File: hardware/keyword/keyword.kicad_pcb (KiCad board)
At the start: 2 copper layers, 42.3 x 19 mm, 60 parts, among them U1 SZYY0402Y_C434450, U11 STM32WB55RGVx, U12 MLPF-WB-04D3, U13 YZ13515055F-02025-02, U15 YZ13515055F-02025-02, U16 XRTC252012S2R2MBCA, U17 SZYY0402Y_C434450, U18 TPS631000DRLR, U2 TPD2EUSB30, U3 NX2012SA-32.768KHZ-STD-MUB-2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

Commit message: add in stuff
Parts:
- added CN1: YZ00615050R-08, TestPoint:TestPoint_Pad_D2.0mm, F.Cu at (205.1, 74.2)
- added CN2: YZ00615050R-08, lcsc:TESTPOINT-SMD_BD2.0-H5.0, F.Cu at (195.2, 74.4)
- added CN3: YZ00615050R-08, lcsc:TESTPOINT-SMD_BD2.0-H5.0, F.Cu at (195.2, 89.8)
- added CN4: YZ00615050R-08, lcsc:TESTPOINT-SMD_BD2.0-H5.0, F.Cu at (179.8, 89.8)
- added CN5: YZ00615050R-08, TestPoint:TestPoint_Pad_D2.0mm, F.Cu at (205.2, 89.6)
- added CN6: YZ00615050R-08, TestPoint:TestPoint_Pad_D2.0mm, F.Cu at (220.6, 89.6)
- added R11: 2.2K, Resistor_SMD:R_0402_1005Metric, F.Cu at (220.6, 81.7)
- added R8: 2.2K, Resistor_SMD:R_0402_1005Metric, F.Cu at (209.1, 89.6)
- added TP6: TestPoint, TestPoint:TestPoint_Pad_D1.5mm, F.Cu at (205.2, 83.7)
- added TP7: TestPoint, TestPoint:TestPoint_Pad_D1.5mm, F.Cu at (205.2, 86.2)
- added TP8: TestPoint, TestPoint:TestPoint_Pad_D1.5mm, F.Cu at (220.6, 83.8)
- added TP9: TestPoint, TestPoint:TestPoint_Pad_D1.5mm, F.Cu at (220.6, 86.3)
- added U19: YZ37215050R-02025-05, lcsc:SMD_2P_YZ37215050R-02025-05, F.Cu at (195.2, 85.2)
- added U20: YZ37215050R-02025-05, lcsc:SMD_2P_YZ37215050R-02025-05, F.Cu at (179.8, 85.2)
- C16, C17, C18, C19, C20, C23, R4, R5, R6, R7, U16, U17, U8: moved to B.Cu
- TP1, TP2, TP3: footprint TestPoint:TestPoint_Pad_D2.0mm -> TestPoint:TestPoint_Pad_D1.5mm; moved to B.Cu
- TP4, TP5: footprint TestPoint:TestPoint_Pad_3.0x3.0mm -> TestPoint:TestPoint_Pad_2.0x2.0mm; moved to B.Cu
- moved TP4 92.4 mm to (185.8, 89.8)
- moved TP5 90.7 mm to (189.2, 89.8), turned to -90 degrees
- moved C35 35.6 mm to (207.9, 84.9), turned to -90 degrees
- moved AE1 23.7 mm to (220.2, 73.5), turned to 0 degrees
- moved C6 18.5 mm to (217.5, 89.5), turned to -135 degrees
- moved C9 18.5 mm to (219.0, 88.0), turned to -135 degrees
- moved U1 17.9 mm to (215.1, 90.4), turned to 180 degrees
- moved TP1 17.2 mm to (205.7, 85.3), turned to 90 degrees
- moved TP2 16.3 mm to (209.1, 89.2), turned to 90 degrees
- moved L2 15.8 mm to (205.8, 77.0), turned to 90 degrees
- moved R3 15.6 mm to (215.7, 88.9), turned to 90 degrees
- moved C36 15.3 mm to (218.9, 85.0), turned to -90 degrees
- moved C32 15.1 mm to (214.0, 73.9), turned to 90 degrees
- moved X1 15.0 mm to (211.3, 74.5), turned to 45 degrees
- moved C31 15.0 mm to (212.1, 89.5), turned to 180 degrees
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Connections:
- U11 pad 5: /BOOT -> unconnected-(U11-PH3-Pad5)
- U11 pad 6: unconnected-(U11-PB8-Pad6) -> /SDA
- U11 pad 7: unconnected-(U11-PB9-Pad7) -> /SCL
- U11 pad 8: /RESET -> unconnected-(U11-NRST-Pad8)
- U13 pad 2: /SDA3 -> /SDA
- U15 pad 1: /SCL3 -> /SCL
- U2 pad 1: /DP -> /DN
- U2 pad 2: /DN -> /DP
- U4 pad 2: /SDA1 -> /SDA
- U5 pad 1: /SCL1 -> /SCL
- U6 pad 2: /SDA2 -> /SDA
- U7 pad 1: /SCL2 -> /SCL
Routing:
- net /SCL: track 0.00 -> 57.1 mm, vias 0 -> 3
- net +3.3V: track 0.00 -> 52.4 mm, vias 0 -> 12
- net /SDA: track 0.00 -> 52.1 mm, vias 0 -> 6
- net VCC: track 0.00 -> 27.6 mm, vias 0 -> 4
- net Net-(C18-Pad1): track 0.00 -> 23.3 mm, vias 0 -> 4
- net GND: track 0.00 -> 18.2 mm, vias 0 -> 33
- net /DP: track 0.00 -> 17.0 mm
- net /DN: track 0.00 -> 16.9 mm
- net Net-(U8-TS): track 0.00 -> 12.4 mm, vias 0 -> 2
- net VBUS: track 0.00 -> 10.0 mm, vias 0 -> 2
- net /HXOUT: track 0.00 -> 6.10 mm
- net /SWCLK: track 0.00 -> 6.06 mm, vias 0 -> 1
- net Net-(C19-Pad1): track 0.00 -> 4.91 mm
- net /SWDIO: track 0.00 -> 4.72 mm, vias 0 -> 1
- net Net-(AE1-ANT): track 0.00 -> 3.86 mm
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- added copper zone on In2.Cu, net +3.3V
- added copper zone on B.Cu, net GND
- added copper zone on F.Cu, net GND
- added copper zone on In1.Cu, net GND
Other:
- board size 42.3 x 19 mm -> 44.4 x 19.2 mm
- copper layers 2 -> 4

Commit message: aa
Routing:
- net +3.3V: track 52.4 -> 53.7 mm, vias 12 -> 13
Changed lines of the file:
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@@
+	)
+	(segment
+		(start 216.9 78.405)
+		(end 216.195 77.7)
+		(width 0.2)
+		(layer "F.Cu")
+		(net 6)
 	)
 	(segment
@@
 	)
 	(segment
+		(start 216.9 78.7)
+		(end 216.9 78.405)
+		(width 0.2)
+		(layer "F.Cu")
+		(net 6)
+	)
+	(segment
 		(start 209.635437 79.661898)
 		(end 209 79.026461)
@@
 	(via
 		(at 218.9 83.7)
+		(size 0.6)
+		(drill 0.3)
+		(layers "F.Cu" "B.Cu")
+		(net 6)
+	)
+	(via
+		(at 216.9 78.7)
 		(size 0.6)
 		(drill 0.3)
@@
 	)
 	(zone
+		(net 2)
+		(net_name "GND")
+		(layer "F.Cu")
+		(name "$teardrop_padvia$")
+		(hatch none 0.1)
+		(priority 30001)
+		(attr
+			(teardrop
+				(type padvia)
+			)
+		)
+		(connect_pads yes
+			(clearance 0)
+		)
+		(min_thickness 0.0254)
+		(filled_areas_thickness no)
+		(fill yes
+			(thermal_gap 0.5)
+			(thermal_bridge_width 0.5)
+			(island_removal_mode 1)
+			(island_area_min 10)
+		)
+		(polygon
+			(pts
+				(xy 213.440898 78.13141) (xy 213.299477 77.989989) (xy 212.783329 78.231446) (xy 212.949293 78.481594)
+				(xy 213.199441 78.647558)
+			)
+		)
+	)
+	(zone
+		(net 2)
+		(net_name "GND")
+		(layer "F.Cu")
+		(name "$teardrop_padvia$")
+		(hatch none 0.1)
+		(priority 30002)
+		(attr
+			(teardrop
+				(type padvia)
+			)
+		)
+		(connect_pads yes
+			(clearance 0)
+		)
+		(min_thickness 0.0254)
+		(filled_areas_thickness no)
+		(fill yes
+			(thermal_gap 0.5)
+			(thermal_bridge_width 0.5)
+			(island_removal_mode 1)
+			(island_area_min 10)
+		)
+		(polygon
+			(pts
+				(xy 213.05 80.737865) (xy 212.85 80.737865) (xy 212.655764 80.802156) (xy 212.95 80.744629) (xy 212.655764 80.802156)
+			)
+		)
+	)
+	(zone
+		(net 2)
+		(net_name "GND")
+		(layer "F.Cu")
+		(name "$teardrop_padvia$")
+		(hatch none 0.1)
+		(priority 30000)
+		(attr
+			(teardrop
+				(type padvia)
+			)
+		)
+		(connect_pads yes
+			(clearance 0)
+		)
+		(min_thickness 0.0254)
+		(filled_areas_thickness no)
+		(fill yes
+			(thermal_gap 0.5)
+			(thermal_bridge_width 0.5)
+			(island_removal_mode 1)
+			(island_area_min 10)
+		)
+		(polygon
+			(pts
+				(xy 212.85 79.075123) (xy 213.05 79.075123) (xy 213.244236 78.539414) (xy 212.95 78.479887) (xy 212.655764 78.539414)
+			)
+		)
+	)
+	(zone

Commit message: finished
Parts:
- removed R3: 150, Resistor_SMD:R_0402_1005Metric
- removed U1: SZYY0402Y_C434450, lcsc:LED0402-FD_YELLOW
- added C3: 100nF, Capacitor_SMD:C_0402_1005Metric, B.Cu at (220.8, 81.9)
- added CN7: YZ00615050R-08, lcsc:TESTPOINT-SMD_BD2.0-H5.0, B.Cu at (205.1, 74.2)
- added CN8: YZ00615050R-08, lcsc:TESTPOINT-SMD_BD2.0-H5.0, B.Cu at (205.2, 89.6)
- added CN9: YZ00615050R-08, lcsc:TESTPOINT-SMD_BD2.0-H5.0, B.Cu at (220.6, 89.6)
- added R12: 100R, Resistor_SMD:R_0402_1005Metric, B.Cu at (210.8, 88.1)
- added R13: 100R, Resistor_SMD:R_0402_1005Metric, B.Cu at (211.1, 86.4)
- added R14: 100R, Resistor_SMD:R_0402_1005Metric, B.Cu at (213.8, 88.9)
- added U10: W25Q16JVUXIQ, lcsc:USON-8_L3.0-W2.0-P0.50-BL-EP, B.Cu at (219.9, 79.7)
- added U14: XL-1608RGBC, lcsc:LED-SMD_4P-L1.6-W0.8-BL, B.Cu at (212.5, 88.7)
- R11, R8: value 2.2K -> 4.7K
- moved R11 16.2 mm to (204.4, 81.5), turned to 90 degrees
- moved R8 8.91 mm to (218.0, 89.9), turned to -90 degrees
- moved U17 5.81 mm to (190.6, 84.6)
- moved C6 2.30 mm to (215.2, 89.4), turned to 180 degrees
- moved AE1 1.23 mm to (219.4, 74.5)
- moved R6 1.00 mm to (191.3, 82.8), turned to 90 degrees
- moved U3 0.91 mm to (216.6, 87.4)
- moved C9 0.77 mm to (218.2, 87.9)
- moved C24 0.25 mm to (208.0, 77.1)
- moved L1 0.25 mm to (208.0, 75.6)
- moved C26 0.20 mm to (207.9, 78.8)
- moved C29 0.20 mm to (207.0, 78.8)
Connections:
- R11 pad 1: /SCL -> /SDA
- R8 pad 1: /SDA -> /SCL
- U11 pad 17: unconnected-(U11-PA2-Pad17) -> /FLASH_NCS
- U11 pad 18: unconnected-(U11-PA3-Pad18) -> /FLASH_CLK
- U11 pad 2: /LED -> unconnected-(U11-PC13-Pad2)
- U11 pad 21: unconnected-(U11-PA6-Pad21) -> /FLASH_IO3
- U11 pad 22: unconnected-(U11-PA7-Pad22) -> /FLASH_IO2
- U11 pad 47: unconnected-(U11-PB13-Pad47) -> /SCL
- U11 pad 48: unconnected-(U11-PB14-Pad48) -> /SDA
- U11 pad 6: /SDA -> /FLASH_IO1
- U11 pad 60: unconnected-(U11-PC12-Pad60) -> /STATUS_B
- U11 pad 61: unconnected-(U11-PD0-Pad61) -> /STATUS_G
- U11 pad 62: unconnected-(U11-PD1-Pad62) -> /STATUS_R
- U11 pad 65: unconnected-(U11-PB5-Pad65) -> /BB_SWIO
- U11 pad 7: /SCL -> /FLASH_IO0
- U8 pad 5: unconnected-(U8-SCL-Pad5) -> /SDA
- U8 pad 6: unconnected-(U8-SDA-Pad6) -> /SCL
- U8 pad 8: unconnected-(U8-OTG-Pad8) -> GND
- U8 pad 9: unconnected-(U8-~{CE}-Pad9) -> GND
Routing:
- net /FLASH_IO0: track 0.00 -> 12.6 mm, vias 0 -> 1
- net Net-(U17-K): track 1.51 -> 12.4 mm, vias 0 -> 2
- net /SDA: track 52.1 -> 61.5 mm, vias 6 -> 5
- net /FLASH_IO1: track 0.00 -> 9.13 mm, vias 0 -> 1
- net /BB_SWIO: track 0.00 -> 7.89 mm, vias 0 -> 1
- net /SCL: track 57.1 -> 64.9 mm
- net /STATUS_B: track 0.00 -> 7.37 mm, vias 0 -> 1
- net +3.3V: track 53.7 -> 59.4 mm, vias 13 -> 15
- net /FLASH_IO3: track 0.00 -> 5.04 mm, vias 0 -> 1
- net /FLASH_CLK: track 0.00 -> 5.01 mm, vias 0 -> 1
- net /STATUS_G: track 0.00 -> 3.58 mm, vias 0 -> 1
- net /LED: track 2.77 -> 0.00 mm
- net /FLASH_NCS: track 0.00 -> 2.09 mm, vias 0 -> 1
- net GND: track 18.2 -> 20.2 mm, vias 33 -> 44
- net /STATUS_R: track 0.00 -> 1.94 mm, vias 0 -> 1
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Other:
- board size 44.4 x 19.2 mm -> 44.4 x 19.3 mm
- board text added: "Keyword"

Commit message: finish case and stuff
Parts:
- TP4, TP5: moved to F.Cu
- moved TP5 13.9 mm to (181.1, 78.5), turned to 90 degrees
- moved TP4 11.2 mm to (186.2, 78.6), turned to -90 degrees
- moved C1 3.16 mm to (206.8, 76.7)
- moved C2 3.16 mm to (206.2, 74.0)
- moved C24 3.16 mm to (204.9, 77.3)
- moved C25 3.16 mm to (213.5, 78.0)
- moved C26 3.16 mm to (204.8, 79.0)
- moved C27 3.16 mm to (211.0, 88.5)
- moved C28 3.16 mm to (202.6, 80.2)
- moved C29 3.16 mm to (203.8, 79.0)
- moved C3 3.16 mm to (217.7, 82.2)
- moved C31 3.16 mm to (209.0, 89.7)
- moved C32 3.16 mm to (210.8, 74.2)
- moved C33 3.16 mm to (210.4, 75.5)
- moved C34 3.16 mm to (214.8, 85.0)
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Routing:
- net Net-(C18-Pad1): track 23.3 -> 9.76 mm, vias 4 -> 3
- net Net-(AE1-ANT): track 2.56 -> 3.30 mm
- net GND: vias 44 -> 45
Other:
- board size 44.4 x 19.3 mm -> 41.3 x 19 mm
- board text added: "+"
- board text added: "-"

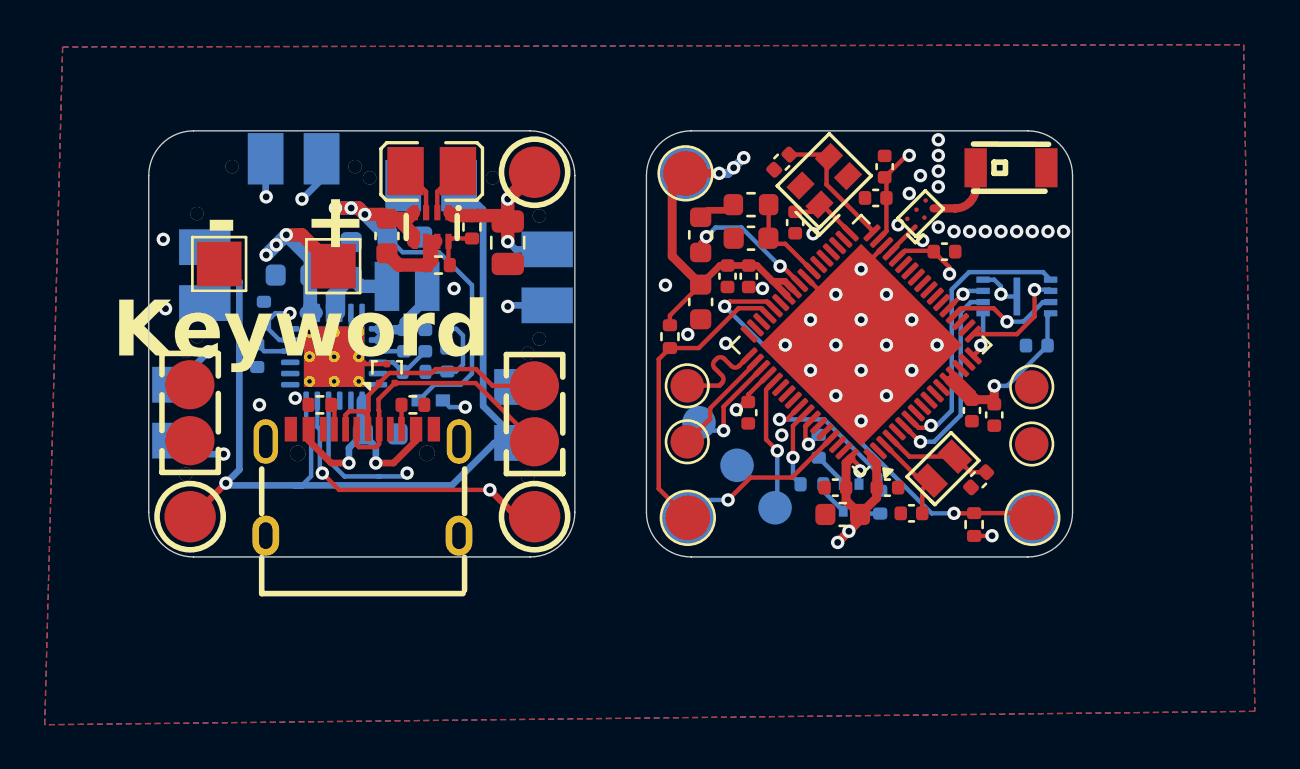
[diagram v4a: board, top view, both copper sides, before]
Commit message: add in mousebites
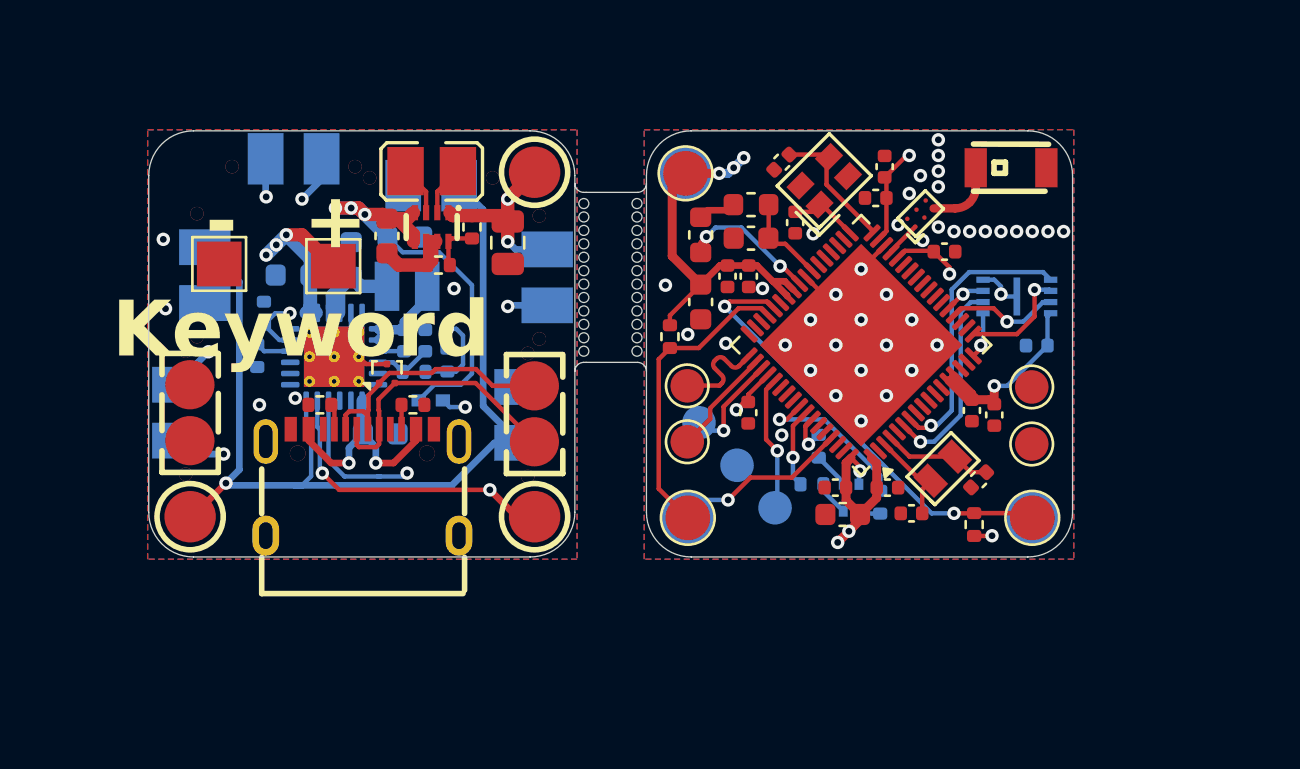
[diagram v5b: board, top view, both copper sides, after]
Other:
- outline, holes or cut-outs redrawn

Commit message: blender and stuff
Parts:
- moved R12 0.54 mm to (207.9, 88.8), turned to 90 degrees
- moved CN1 0.15 mm to (201.9, 74.3)
- moved CN7 0.15 mm to (201.9, 74.3)
- moved CN4 0.11 mm to (179.7, 89.8)
- moved CN2 0.11 mm to (195.2, 74.3)
- moved CN5 0.10 mm to (201.9, 89.8)
- moved CN8 0.10 mm to (201.9, 89.8)
- moved CN3 0.07 mm to (195.2, 89.8)
- moved CN6 0.05 mm to (217.5, 89.8)
- moved CN9 0.05 mm to (217.5, 89.8)
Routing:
- net +3.3V: track 59.4 -> 60.1 mm
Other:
- outline, holes or cut-outs redrawn
